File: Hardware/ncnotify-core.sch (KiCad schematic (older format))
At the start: 48 parts, among them J1 5-1634503-1, J2 67996-412HLF, J3 USB4110-GF-A, J4 Conn_ARM_JTAG_SWD_10, Q1 NX3008NBKS, SW1 SW_Push, SW2 SW_Push, U1 STM32L422CBT6, U2 TLV71333PDBV, X1 SMTU1632-LF, Y1 Q13FC1350000400

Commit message: Remove switches and expansion header
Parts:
- removed J2: 67996-412HLF, digikey-footprints:PinHeader_6x2_P2.54mm_Vertical, symbol dk_Rectangular-Connectors-Headers-Male-Pins:67996-412HLF
- removed JP4: Jumper_2_Open, Connector_PinHeader_2.54mm:PinHeader_1x02_P2.54mm_Vertical, symbol Jumper:Jumper_2_Open
- removed R11, R12: 5k1, Resistor_SMD:R_0402_1005Metric, symbol Device:R_US
- removed S1: ZMSL03130T10LLC, ncnotify-core:ZMSL03130T10LLC, symbol nc-core-collection:ZMSL03130T10LLC
- J4: footprint Connector_PinHeader_1.27mm:PinHeader_2x05_P1.27mm_Vertical -> Connector_PinHeader_1.27mm:PinHeader_2x05_P1.27mm_Vertical_SMD
- R9: DNF (none) -> DNF
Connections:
- wire segments 125 -> 112
- no-connect marks 22 -> 28
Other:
- moved on the sheet: R9
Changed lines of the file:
@@
 Wire Wire Line
 	2000 5400 2000 5250
-$Comp
-L nc-core-collection:ZMSL03130T10LLC S1
-U 1 1 5FAD4FED
-P 4000 5000
-F 0 "S1" V 3585 4604 50  0000 C CNN
-F 1 "ZMSL03130T10LLC" V 3676 4604 50  0000 C CNN
-F 2 "ncnotify-core:ZMSL03130T10LLC" H 4000 5000 50  0001 C CNN
-F 3 "" H 4000 5000 50  0001 C CNN
-	1    4000 5000
-	0    1    1    0
-$EndComp
 Wire Wire Line
 	2000 5400 3200 5400
@@
 Power (USB/Batt)
 Wire Wire Line
-	2000 4350 3000 4350
-Wire Wire Line
-	3550 5150 3200 5150
-Wire Wire Line
-	3200 5150 3200 5400
-Wire Wire Line
-	3000 5000 3000 4350
-Wire Wire Line
-	3000 5000 3550 5000
-Connection ~ 3000 4350
-Wire Wire Line
-	3000 4350 3350 4350
-Wire Wire Line
 	2000 4850 3150 4850
 Wire Wire Line
 	3150 4750 3150 4850
-Connection ~ 3150 4850
-Wire Wire Line
-	3150 4850 3550 4850
 $Comp
 L Device:R_US R1
@@
 F 0 "J4" V 4260 6946 50  0000 R CNN
 F 1 "Conn_ARM_JTAG_SWD_10" V 4159 7352 50  0000 R CNN
-F 2 "Connector_PinHeader_1.27mm:PinHeader_2x05_P1.27mm_Vertical" H 4700 6900 50  0001 C CNN
+F 2 "Connector_PinHeader_1.27mm:PinHeader_2x05_P1.27mm_Vertical_SMD" H 4700 6900 50  0001 C CNN
 F 3 "http://infocenter.arm.com/help/topic/com.arm.doc.ddi0314h/DDI0314H_coresight_components_trm.pdf" V 4350 5650 50  0001 C CNN
 	1    4700 6900
@@
 	10650 4600 10650 4700
 Connection ~ 10650 4700
-Wire Wire Line
-	8550 5200 8550 4950
 Text GLabel 8550 2600 0    50   Input ~ 0
 SENSE_IN
@@
 Wire Notes Line
 	5100 2350 5100 650
-$Comp
-L Device:R_US R9
-U 1 1 5FB99AFF
-P 8550 5350
-F 0 "R9" H 8618 5396 50  0000 L CNN
-F 1 "51k" H 8618 5305 50  0000 L CNN
-F 2 "Resistor_SMD:R_0402_1005Metric" V 8590 5340 50  0001 C CNN
-F 3 "~" H 8550 5350 50  0001 C CNN
-	1    8550 5350
-	1    0    0    -1
-$EndComp
-Connection ~ 8300 5500
 Wire Wire Line
 	8550 5500 8300 5500
@@
 	1    8300 5900
 	1    0    0    -1
-$EndComp
-$Comp
-L Jumper:Jumper_2_Open JP4
-U 1 1 5FB7B1BB
-P 8300 5300
-F 0 "JP4" H 8300 5535 50  0000 C CNN
-F 1 "Jumper_2_Open" H 8300 5444 50  0000 C CNN
-F 2 "Connector_PinHeader_2.54mm:PinHeader_1x02_P2.54mm_Vertical" H 8300 5300 50  0001 C CNN
-F 3 "~" H 8300 5300 50  0001 C CNN
-	1    8300 5300
-	0    -1   -1   0
 $EndComp
 $Comp
@@
 Text GLabel 10550 3950 2    50   Input ~ 0
 SPI2_SS_0
-$Comp
-L dk_Rectangular-Connectors-Headers-Male-Pins:67996-412HLF J2
-U 1 1 5FBDB51C
-P 5700 4900
-F 0 "J2" V 5753 4522 60  0000 R CNN
-F 1 "67996-412HLF" V 5647 4522 60  0000 R CNN
-F 2 "digikey-footprints:PinHeader_6x2_P2.54mm_Vertical" H 5900 5100 60  0001 L CNN
-F 3 "https://cdn.amphenol-icc.com/media/wysiwyg/files/drawing/67996.pdf" H 5900 5200 60  0001 L CNN
-F 4 "609-3219-ND" H 5900 5300 60  0001 L CNN "Digi-Key_PN"
-F 5 "67996-412HLF" H 5900 5400 60  0001 L CNN "MPN"
-F 6 "Connectors, Interconnects" H 5900 5500 60  0001 L CNN "Category"
-F 7 "Rectangular Connectors - Headers, Male Pins" H 5900 5600 60  0001 L CNN "Family"
-F 8 "https://cdn.amphenol-icc.com/media/wysiwyg/files/drawing/67996.pdf" H 5900 5700 60  0001 L CNN "DK_Datasheet_Link"
-F 9 "/product-detail/en/amphenol-icc-fci/67996-412HLF/609-3219-ND/1878508" H 5900 5800 60  0001 L CNN "DK_Detail_Page"
-F 10 "CONN HEADER VERT 12POS 2.54MM" H 5900 5900 60  0001 L CNN "Description"
-F 11 "Amphenol ICC (FCI)" H 5900 6000 60  0001 L CNN "Manufacturer"
-F 12 "Active" H 5900 6100 60  0001 L CNN "Status"
-	1    5700 4900
-	0    -1   -1   0
-$EndComp
-Wire Wire Line
-	5500 5100 5500 4700
-Wire Wire Line
-	5600 5100 5600 4700
-$Comp
-L power:GND #PWR020
-U 1 1 5FC160C9
-P 5600 5100
-F 0 "#PWR020" H 5600 4850 50  0001 C CNN
-F 1 "GND" H 5605 4927 50  0000 C CNN
-F 2 "" H 5600 5100 50  0001 C CNN
-F 3 "" H 5600 5100 50  0001 C CNN
-	1    5600 5100
-	1    0    0    -1
-$EndComp
-Connection ~ 5600 5100
-$Comp
-L power:VDD #PWR016
-U 1 1 5FC19D45
-P 5500 4700
-F 0 "#PWR016" H 5500 4550 50  0001 C CNN
-F 1 "VDD" H 5515 4873 50  0000 C CNN
-F 2 "" H 5500 4700 50  0001 C CNN
-F 3 "" H 5500 4700 50  0001 C CNN
-	1    5500 4700
-	1    0    0    -1
-$EndComp
-Connection ~ 5500 4700
 Text GLabel 5800 5100 3    50   Input ~ 0
 I2C1_SCL
@@
 Wire Wire Line
 	900  7500 3150 7500
+Text GLabel 4850 3350 0    50   Input ~ 0
+D+
 Text GLabel 4850 3050 0    50   Input ~ 0
-D+
-Text GLabel 4850 3350 0    50   Input ~ 0
 D-
 $Comp
@@
 	3850 1700 3650 1700
 Connection ~ 3650 1700
-$Comp
-L Device:R_US R11
-U 1 1 5FB708BB
-P 9750 5850
-F 0 "R11" H 9818 5896 50  0000 L CNN
-F 1 "5k1" H 9818 5805 50  0000 L CNN
-F 2 "Resistor_SMD:R_0402_1005Metric" V 9790 5840 50  0001 C CNN
-F 3 "~" H 9750 5850 50  0001 C CNN
-	1    9750 5850
-	1    0    0    -1
-$EndComp
-$Comp
-L Device:R_US R12
-U 1 1 5FB70F30
-P 10150 5850
-F 0 "R12" H 10218 5896 50  0000 L CNN
-F 1 "5k1" H 10218 5805 50  0000 L CNN
-F 2 "Resistor_SMD:R_0402_1005Metric" V 10190 5840 50  0001 C CNN
-F 3 "~" H 10150 5850 50  0001 C CNN
-	1    10150 5850
-	1    0    0    -1
-$EndComp
-Wire Wire Line
-	9750 5700 9750 5600
-Wire Wire Line
-	9750 5600 9950 5600
-Wire Wire Line
-	10150 5600 10150 5700
-Wire Wire Line
-	9950 5600 9950 5500
-Connection ~ 9950 5600
-Wire Wire Line
-	9950 5600 10150 5600
-$Comp
-L power:VDD #PWR024
-U 1 1 5FB7A979
-P 9950 5500
-F 0 "#PWR024" H 9950 5350 50  0001 C CNN
-F 1 "VDD" H 9965 5673 50  0000 C CNN
-F 2 "" H 9950 5500 50  0001 C CNN
-F 3 "" H 9950 5500 50  0001 C CNN
-	1    9950 5500
-	1    0    0    -1
-$EndComp
-Text GLabel 10150 6150 2    50   Input ~ 0
-I2C1_SCL
-Text GLabel 9750 6150 0    50   Input ~ 0
-I2C1_SDA
-Wire Wire Line
-	9750 6000 9750 6150
-Wire Wire Line
-	10150 6150 10150 6000
 Wire Wire Line
 	1500 4750 1500 4800
@@
 Wire Notes Line
 	7750 650  5100 650
+Wire Wire Line
+	2000 4350 3350 4350
+NoConn ~ 5700 4700
+NoConn ~ 5800 4700
+NoConn ~ 5900 4700
+NoConn ~ 6000 4700
+NoConn ~ 5800 5100
+NoConn ~ 5700 5100
+Wire Wire Line
+	8300 5100 8300 5150
+Wire Wire Line
+	8300 5450 8300 5500
+Connection ~ 8300 5500
+Wire Wire Line
+	8550 4950 8550 5500
+$Comp
+L Device:R_US R9
+U 1 1 5FB99AFF
+P 8300 5300
+F 0 "R9" H 8368 5346 50  0000 L CNN
+F 1 "51k" H 8368 5255 50  0000 L CNN
+F 2 "Resistor_SMD:R_0402_1005Metric" V 8340 5290 50  0001 C CNN
+F 3 "~" H 8300 5300 50  0001 C CNN
+F 4 "DNF" H 8300 5300 50  0000 C CNN "DNF"
+	1    8300 5300
+	1    0    0    -1
+$EndComp
 $EndSCHEMATC

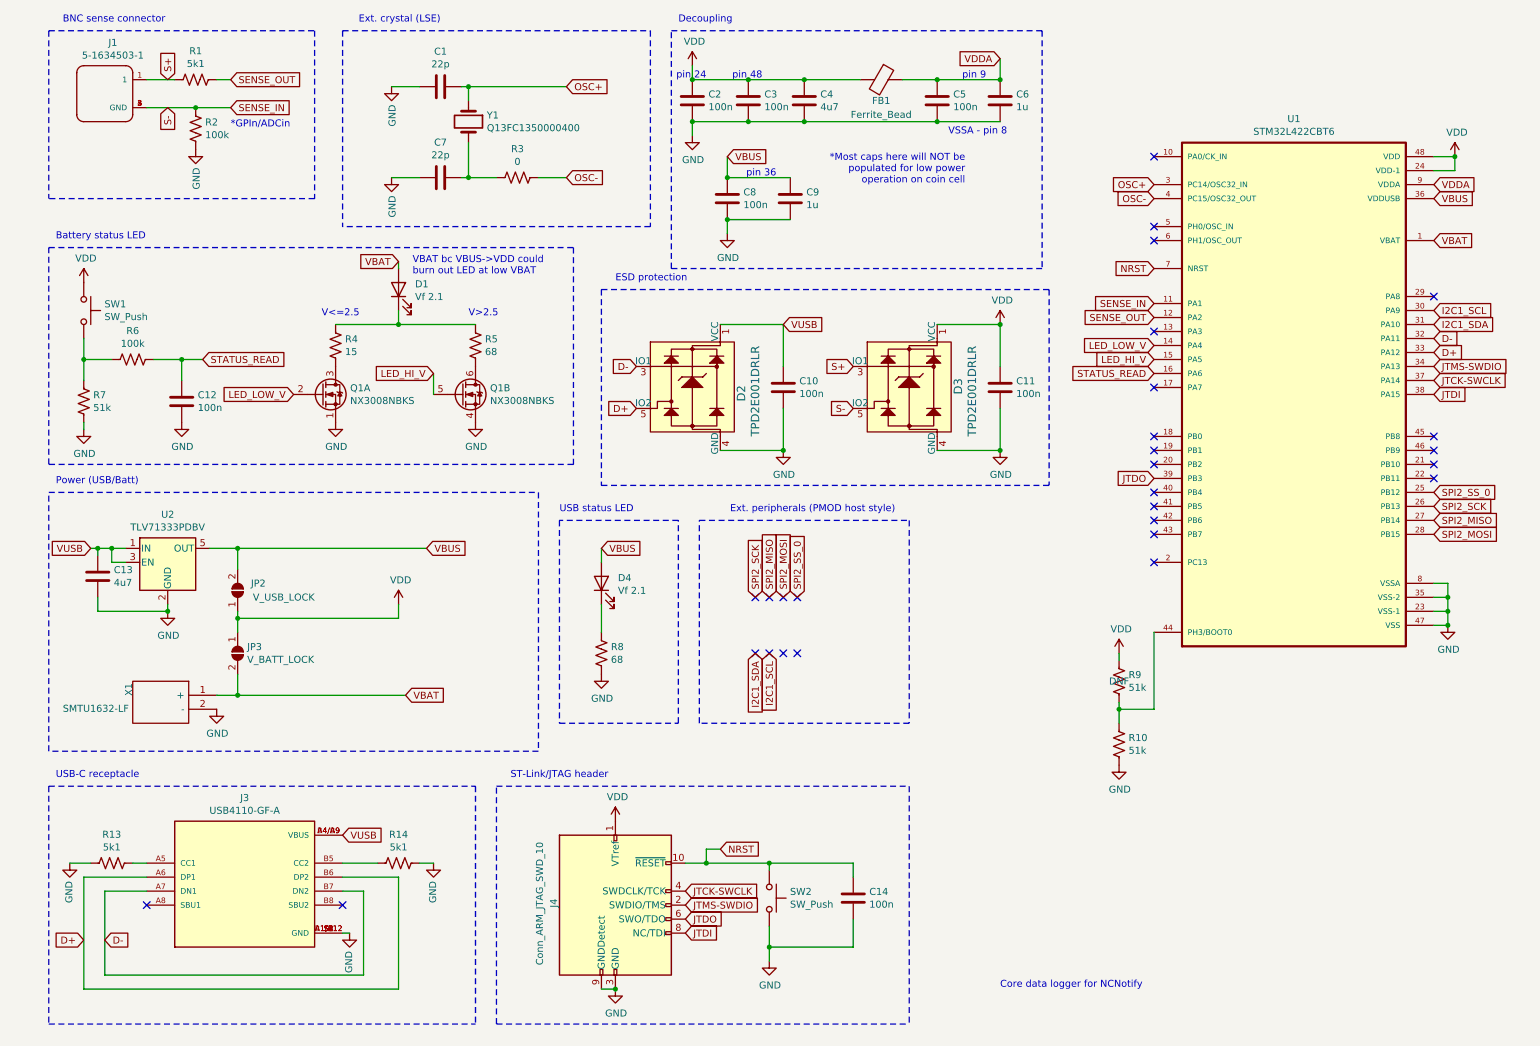
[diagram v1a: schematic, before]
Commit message: Routing and replaced USB ESD chip
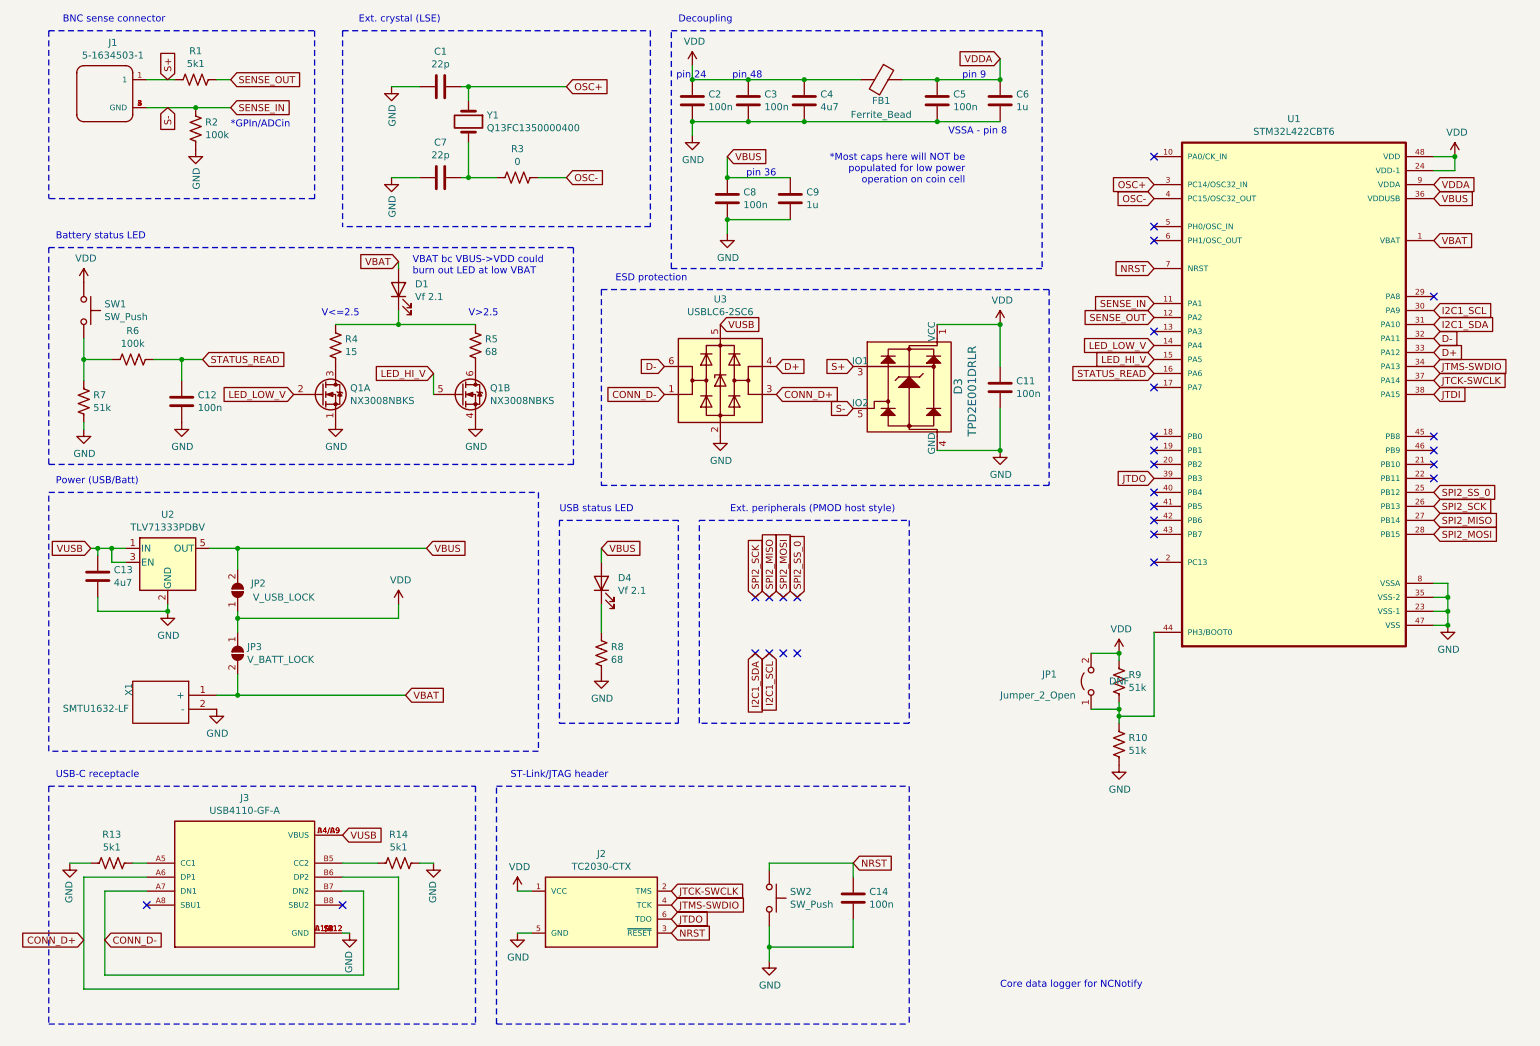
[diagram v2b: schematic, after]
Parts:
- removed C10: 100n, Capacitor_SMD:C_0402_1005Metric, symbol Device:C
- removed D2: TPD2E001DRLR, digikey-footprints:SOT-553, symbol dk_TVS-Diodes:TPD2E001DRLR
- removed J4: Conn_ARM_JTAG_SWD_10, Connector_PinHeader_1.27mm:PinHeader_2x05_P1.27mm_Vertical_SMD, symbol Connector:Conn_ARM_JTAG_SWD_10
- added J2: TC2030-CTX, libs:TC2030-IDC-NL, symbol TC2030-CTX:TC2030-CTX
- added JP1: Jumper_2_Open, Connector_PinHeader_1.27mm:PinHeader_1x02_P1.27mm_Vertical, symbol Jumper:Jumper_2_Open
- added U3: USBLC6-2SC6, Package_TO_SOT_SMD:SOT-23-6, symbol Power_Protection:USBLC6-2SC6
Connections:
- net D+: now also U3.4 (I/O2); no longer J3.A6 (DP1), J3.B6 (DP2)
- net D-: now also U3.6 (I/O1); no longer J3.A7 (DN1), J3.B7 (DN2)
- net GND: now also J2.5 (GND), U3.2 (GND)
- net JTCK-SWCLK: now also J2.2 (TMS)
- net JTDO: now also J2.6 (TDO)
- net JTMS-SWDIO: now also J2.4 (TCK)
- net NRST: now also J2.3 (~RESET)
- net VDD: now also J2.1 (VCC), JP1.2 (B)
- net VUSB: now also U3.5 (VBUS)
- net at R10.1, R9.2, U1.44 (PH3/BOOT0): now also JP1.1 (A)
- new net CONN_D+: J3.A6 (DP1), J3.B6 (DP2), U3.3 (I/O2)
- new net CONN_D-: J3.A7 (DN1), J3.B7 (DN2), U3.1 (I/O1)
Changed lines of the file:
@@
 $EndComp
 Text GLabel 900  7150 0    50   Input ~ 0
-D+
+CONN_D+
 Text GLabel 1050 7150 2    50   Input ~ 0
-D-
+CONN_D-
 Wire Wire Line
 	1350 6800 1050 6800
@@
 Wire Notes Line
 	650  650  2550 650
-$Comp
-L Connector:Conn_ARM_JTAG_SWD_10 J4
-U 1 1 5FB2A1CF
-P 4700 6900
-F 0 "J4" V 4260 6946 50  0000 R CNN
-F 1 "Conn_ARM_JTAG_SWD_10" V 4159 7352 50  0000 R CNN
-F 2 "Connector_PinHeader_1.27mm:PinHeader_2x05_P1.27mm_Vertical_SMD" H 4700 6900 50  0001 C CNN
-F 3 "http://infocenter.arm.com/help/topic/com.arm.doc.ddi0314h/DDI0314H_coresight_components_trm.pdf" V 4350 5650 50  0001 C CNN
-	1    4700 6900
-	1    0    0    -1
-$EndComp
-Text GLabel 5200 6900 2    50   Input ~ 0
+Text GLabel 5100 6900 2    50   Input ~ 0
 JTMS-SWDIO
 Text GLabel 10550 3050 2    50   Input ~ 0
@@
 Text GLabel 10550 3150 2    50   Input ~ 0
 JTCK-SWCLK
-Text GLabel 5200 6800 2    50   Input ~ 0
+Text GLabel 5100 6800 2    50   Input ~ 0
 JTCK-SWCLK
-Text GLabel 5200 7100 2    50   Input ~ 0
-JTDI
 Text GLabel 10550 3250 2    50   Input ~ 0
 JTDI
-Text GLabel 5200 7000 2    50   Input ~ 0
+Text GLabel 5100 7000 2    50   Input ~ 0
 JTDO
 Text GLabel 8550 3850 0    50   Input ~ 0
 JTDO
-Text GLabel 5450 6500 2    50   Input ~ 0
+Text GLabel 6400 6600 2    50   Input ~ 0
 NRST
 Text GLabel 8550 2350 0    50   Input ~ 0
@@
 L power:VDD #PWR026
 U 1 1 5FB3E2D3
-P 4700 6300
-F 0 "#PWR026" H 4700 6150 50  0001 C CNN
-F 1 "VDD" H 4715 6473 50  0000 C CNN
-F 2 "" H 4700 6300 50  0001 C CNN
-F 3 "" H 4700 6300 50  0001 C CNN
-	1    4700 6300
+P 4000 6800
+F 0 "#PWR026" H 4000 6650 50  0001 C CNN
+F 1 "VDD" H 4015 6973 50  0000 C CNN
+F 2 "" H 4000 6800 50  0001 C CNN
+F 3 "" H 4000 6800 50  0001 C CNN
+	1    4000 6800
 	1    0    0    -1
 $EndComp
@@
 L power:GND #PWR031
 U 1 1 5FB3FA87
-P 4700 7500
-F 0 "#PWR031" H 4700 7250 50  0001 C CNN
-F 1 "GND" H 4705 7327 50  0000 C CNN
-F 2 "" H 4700 7500 50  0001 C CNN
-F 3 "" H 4700 7500 50  0001 C CNN
-	1    4700 7500
-	1    0    0    -1
-$EndComp
-Wire Wire Line
-	4600 7500 4700 7500
-Connection ~ 4700 7500
+P 4000 7100
+F 0 "#PWR031" H 4000 6850 50  0001 C CNN
+F 1 "GND" H 4005 6927 50  0000 C CNN
+F 2 "" H 4000 7100 50  0001 C CNN
+F 3 "" H 4000 7100 50  0001 C CNN
+	1    4000 7100
+	1    0    0    -1
+$EndComp
+Wire Wire Line
+	4000 7100 4100 7100
 Wire Notes Line
 	3850 7750 3850 6050
 Text Notes 5150 600  0    50   ~ 0
 Decoupling
-Connection ~ 5800 6600
-Wire Wire Line
-	5200 6600 5350 6600
-Wire Wire Line
-	5450 6500 5350 6500
-Wire Wire Line
-	5350 6500 5350 6600
-Connection ~ 5350 6600
-Wire Wire Line
-	5350 6600 5800 6600
 $Comp
 L power:GND #PWR019
@@
 	5100 2350 5100 650
 Wire Wire Line
-	8550 5500 8300 5500
-Wire Wire Line
-	8300 5500 8300 5600
+	8300 5500 8300 5550
 $Comp
 L power:VDD #PWR021
@@
 	650  6050 650  7750
 $Comp
-L dk_TVS-Diodes:TPD2E001DRLR D2
-U 1 1 5FC826E5
-P 5250 3150
-F 0 "D2" V 5600 3000 60  0000 L CNN
-F 1 "TPD2E001DRLR" V 5700 2750 60  0000 L CNN
-F 2 "digikey-footprints:SOT-553" H 5450 3350 60  0001 L CNN
-F 3 "http://www.ti.com/general/docs/suppproductinfo.tsp?distId=10&gotoUrl=http%3A%2F%2Fwww.ti.com%2Flit%2Fgpn%2Ftpd2e001" H 5450 3450 60  0001 L CNN
-F 4 "296-21883-1-ND" H 5450 3550 60  0001 L CNN "Digi-Key_PN"
-F 5 "TPD2E001DRLR" H 5450 3650 60  0001 L CNN "MPN"
-F 6 "Circuit Protection" H 5450 3750 60  0001 L CNN "Category"
-F 7 "TVS - Diodes" H 5450 3850 60  0001 L CNN "Family"
-F 8 "http://www.ti.com/general/docs/suppproductinfo.tsp?distId=10&gotoUrl=http%3A%2F%2Fwww.ti.com%2Flit%2Fgpn%2Ftpd2e001" H 5450 3950 60  0001 L CNN "DK_Datasheet_Link"
-F 9 "/product-detail/en/texas-instruments/TPD2E001DRLR/296-21883-1-ND/1629242" H 5450 4050 60  0001 L CNN "DK_Detail_Page"
-F 10 "TVS DIODE 5.5V SOT5" H 5450 4150 60  0001 L CNN "Description"
-F 11 "Texas Instruments" H 5450 4250 60  0001 L CNN "Manufacturer"
-F 12 "Active" H 5450 4350 60  0001 L CNN "Status"
-	1    5250 3150
-	1    0    0    -1
-$EndComp
-$Comp
 L dk_TVS-Diodes:TPD2E001DRLR D3
 U 1 1 5FC82B04
@@
 Wire Wire Line
 	900  7500 3150 7500
-Text GLabel 4850 3350 0    50   Input ~ 0
+Text GLabel 5850 3050 2    50   Input ~ 0
 D+
-Text GLabel 4850 3050 0    50   Input ~ 0
+Text GLabel 5050 3050 0    50   Input ~ 0
 D-
 $Comp
 L power:GND #PWR014
 U 1 1 5FC93372
-P 5900 3650
-F 0 "#PWR014" H 5900 3400 50  0001 C CNN
-F 1 "GND" H 5905 3477 50  0000 C CNN
-F 2 "" H 5900 3650 50  0001 C CNN
-F 3 "" H 5900 3650 50  0001 C CNN
-	1    5900 3650
+P 5450 3550
+F 0 "#PWR014" H 5450 3300 50  0001 C CNN
+F 1 "GND" H 5455 3377 50  0000 C CNN
+F 2 "" H 5450 3550 50  0001 C CNN
+F 3 "" H 5450 3550 50  0001 C CNN
+	1    5450 3550
 	1    0    0    -1
 $EndComp
@@
 $EndComp
 $Comp
-L Device:C C10
-U 1 1 5FC981CC
-P 5900 3200
-F 0 "C10" H 6015 3246 50  0000 L CNN
-F 1 "100n" H 6015 3155 50  0000 L CNN
-F 2 "Capacitor_SMD:C_0402_1005Metric" H 5938 3050 50  0001 C CNN
-F 3 "~" H 5900 3200 50  0001 C CNN
-	1    5900 3200
-	1    0    0    -1
-$EndComp
-$Comp
 L Device:C C11
 U 1 1 5FC9851F
@@
 	1    0    0    -1
 $EndComp
-Text GLabel 5900 2750 2    50   Input ~ 0
+Text GLabel 5450 2750 2    50   Input ~ 0
 VUSB
 $Comp
@@
 $EndComp
 Wire Wire Line
-	5900 3650 5900 3350
-Wire Wire Line
-	5900 3050 5900 2750
-Wire Wire Line
-	5450 2750 5900 2750
-Wire Wire Line
 	7000 2750 7450 2750
-Connection ~ 5900 3650
-Wire Wire Line
-	5450 3650 5900 3650
 Wire Wire Line
 	7000 3650 7450 3650
@@
 	8300 5450 8300 5500
 Connection ~ 8300 5500
-Wire Wire Line
-	8550 4950 8550 5500
 $Comp
 L Device:R_US R9
@@
 	1    0    0    -1
 $EndComp
+$Comp
+L TC2030-CTX:TC2030-CTX J2
+U 1 1 5FC452D4
+P 4600 6900
+F 0 "J2" H 4600 7267 50  0000 C CNN
+F 1 "TC2030-CTX" H 4600 7176 50  0000 C CNN
+F 2 "libs:TC2030-IDC-NL" H 4600 6900 50  0001 C CNN
+F 3 "" H 4600 6900 50  0001 L BNN
+	1    4600 6900
+	1    0    0    -1
+$EndComp
+Wire Wire Line
+	4000 6800 4100 6800
+Text GLabel 5100 7100 2    50   Input ~ 0
+NRST
+$Comp
+L Jumper:Jumper_2_Open JP1
+U 1 1 5FC6DA81
+P 8100 5300
+F 0 "JP1" V 8150 5650 50  0000 R CNN
+F 1 "Jumper_2_Open" V 8000 5950 50  0000 R CNN
+F 2 "Connector_PinHeader_1.27mm:PinHeader_1x02_P1.27mm_Vertical" H 8100 5300 50  0001 C CNN
+F 3 "~" H 8100 5300 50  0001 C CNN
+	1    8100 5300
+	0    -1   -1   0
+$EndComp
+Wire Wire Line
+	8100 5500 8300 5500
+Wire Wire Line
+	8300 5550 8550 5550
+Connection ~ 8300 5550
+Wire Wire Line
+	8300 5550 8300 5600
+Wire Wire Line
+	8550 4950 8550 5550
+Wire Wire Line
+	8100 5100 8300 5100
+Connection ~ 8300 5100
+$Comp
+L Power_Protection:USBLC6-2SC6 U3
+U 1 1 5FD3B7E9
+P 5450 3150
+F 0 "U3" H 5450 3731 50  0000 C CNN
+F 1 "USBLC6-2SC6" H 5450 3640 50  0000 C CNN
+F 2 "Package_TO_SOT_SMD:SOT-23-6" H 5450 2650 50  0001 C CNN
+F 3 "https://www.st.com/resource/en/datasheet/usblc6-2.pdf" H 5650 3500 50  0001 C CNN
+	1    5450 3150
+	1    0    0    -1
+$EndComp
+Text GLabel 5850 3250 2    50   Input ~ 0
+CONN_D+
+Text GLabel 5050 3250 0    50   Input ~ 0
+CONN_D-
 $EndSCHEMATC
